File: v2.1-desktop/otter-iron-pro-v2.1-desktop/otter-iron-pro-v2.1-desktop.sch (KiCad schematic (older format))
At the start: 73 parts, among them J1 C167321, J2 +24V, J3 GND, J4 SSD1306, J5 OLED_64x32, J6 SWD, J7 C245, J8 +24V, J9 GND, Q1 SS8050, Q2 SS8050, Q3 BC807, Q4 NCE40P70K or DMP4015SK3Q-13 o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, SW1 key2, SW2 key1, U1 AP2204R-3.3, U2 USBLC6-4SC6, U3 STUSB4500QTR, U4 STM32F072C8Tx, U5 SI8540, U6 OPA340NA, U7 MCP9700AT-ETT

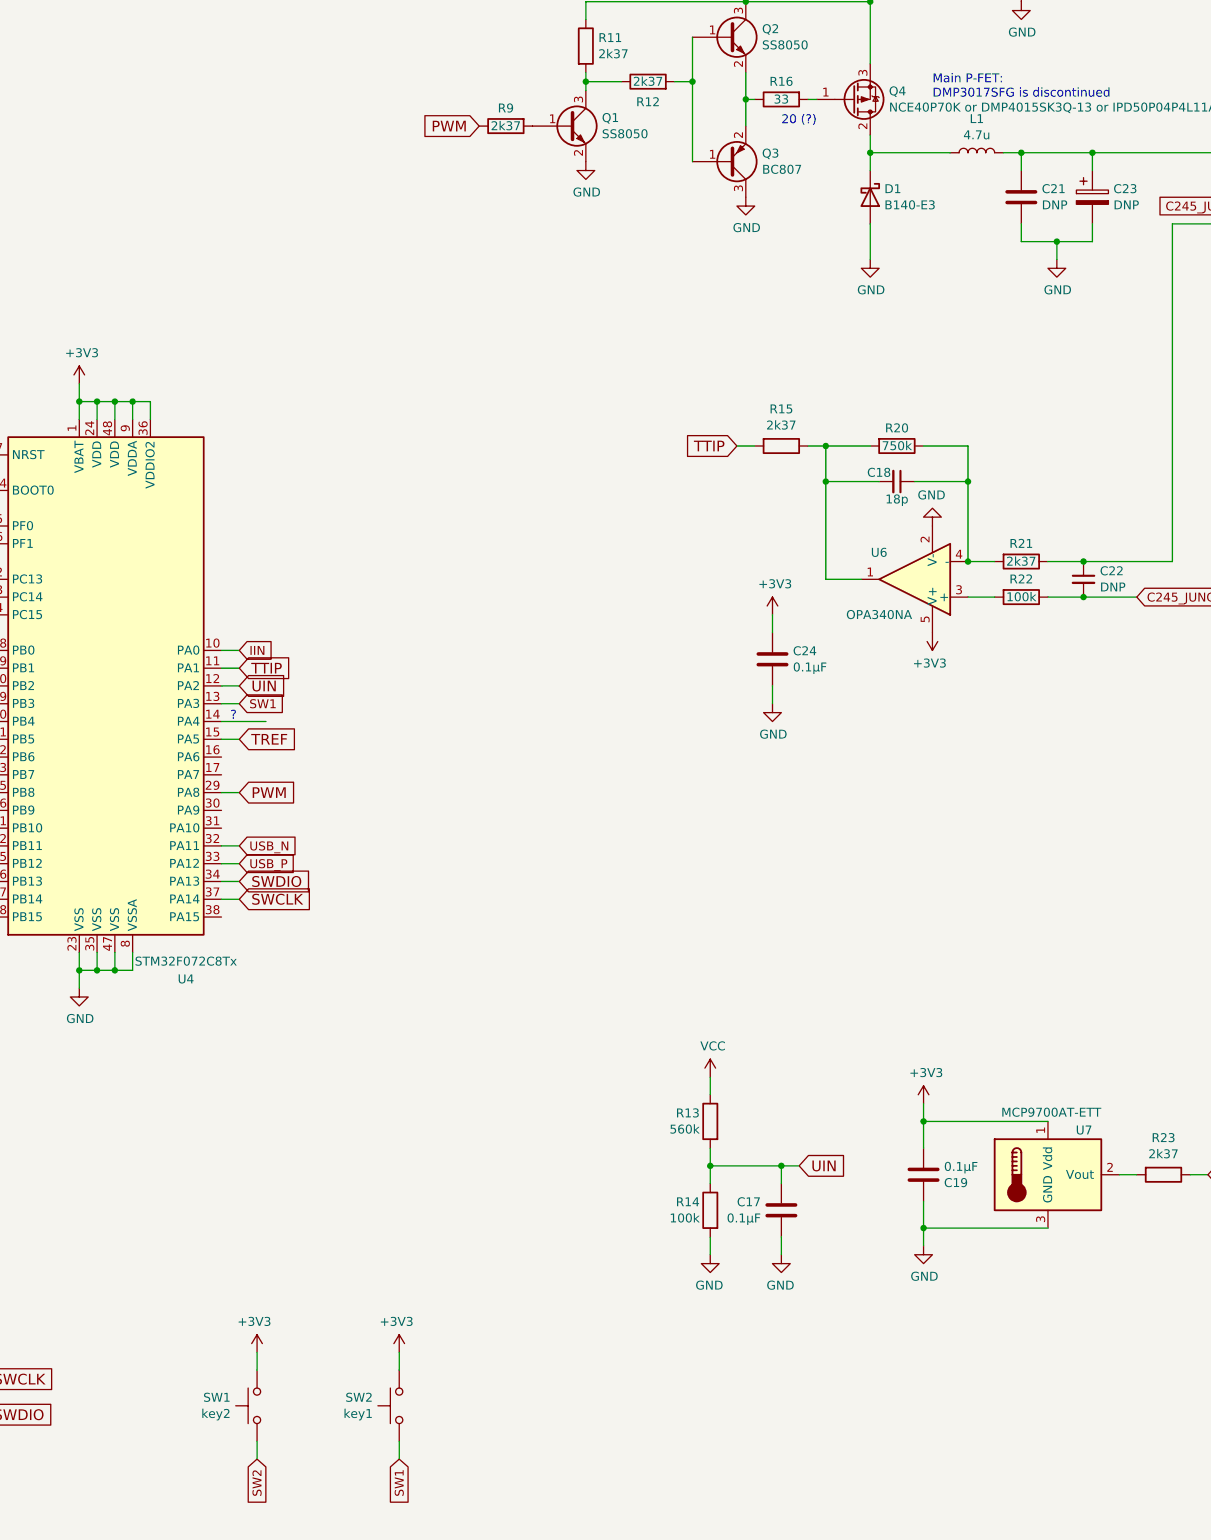
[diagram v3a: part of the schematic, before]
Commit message: Export gerbers; Add LCSC part numbers
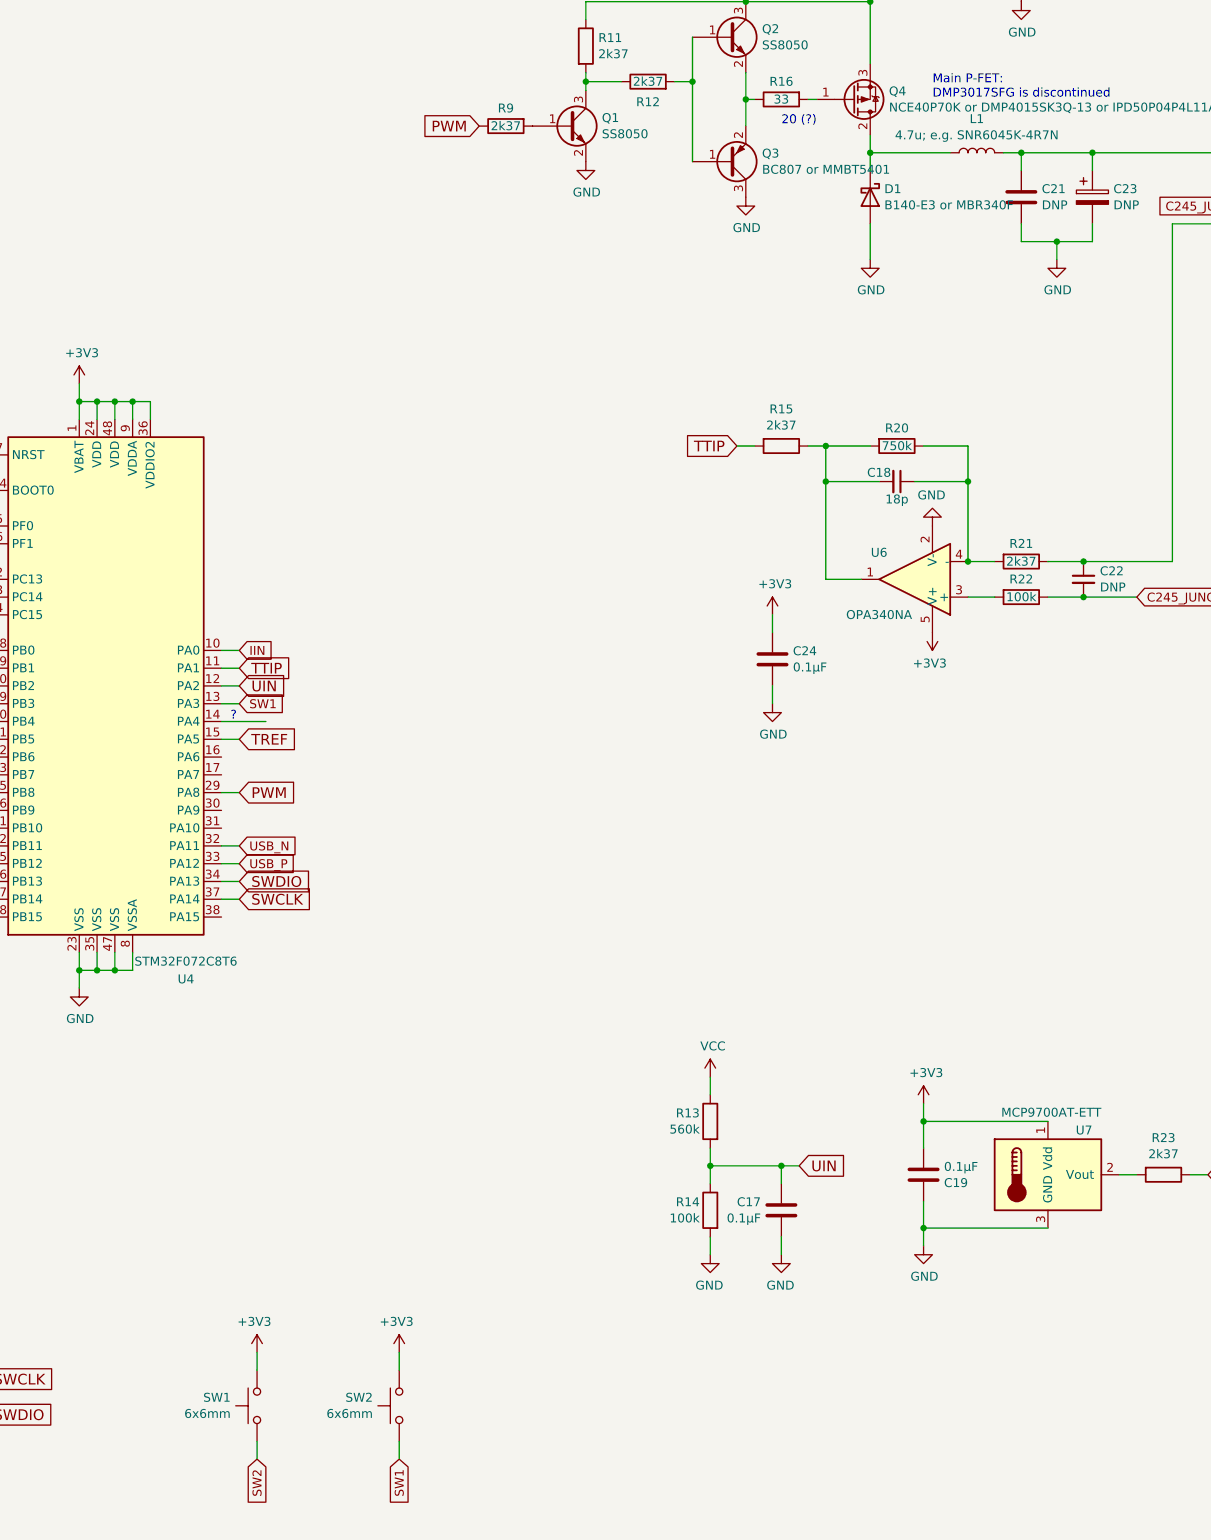
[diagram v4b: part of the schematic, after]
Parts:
- C1, C12, C13, C14, C15, C2, C4, C6, C7, C8: LCSC (none) -> C115388
- C10, C11, C16, C17, C19, C24, C3, C5, C9: LCSC (none) -> C30926
- C18: LCSC (none) -> C126551
- C20: LCSC (none) -> C178713
- D1: value B140-E3 -> B140-E3 or MBR340F; LCSC (none) -> C475721
- F1: LCSC (none) -> C58066
- J1: LCSC (none) -> C167321
- L1: value 4.7u -> 4.7u; e.g. SNR6045K-4R7N; LCSC (none) -> C326336
- Q1, Q2: LCSC (none) -> C2150
- Q3: value BC807 -> BC807 or MMBT5401; LCSC (none) -> C8326
- Q4: LCSC (none) -> C130101
- R1, R10, R11, R12, R15, R21, R23, R3, R4, R5, R6, R7, R8, R9: LCSC (none) -> C25964
- R13, R2: LCSC (none) -> C23203
- R14, R22: LCSC (none) -> C15458
- R16, R17, R18: LCSC (none) -> C23140
- R19: LCSC (none) -> C104920
- R20: LCSC (none) -> C26005
- SW1: value key2 -> 6x6mm; LCSC (none) -> C493026
- SW2: value key1 -> 6x6mm; LCSC (none) -> C493026
- U1: LCSC (none) -> C156303
- U2: LCSC (none) -> C111212
- U3: LCSC (none) -> C506650
- U4: value STM32F072C8Tx -> STM32F072C8T6; LCSC (none) -> C80488
- U6: LCSC (none) -> C73479
- U7: LCSC (none) -> C127949
